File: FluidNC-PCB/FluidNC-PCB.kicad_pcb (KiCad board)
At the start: 2 copper layers, 133 x 92.5 mm, 51 parts, among them J1 Conn_01x04_Pin, J11 Molex_01x02_Socket, J12 Molex_01x02_Socket, J13 Molex_01x02_Socket, J14 Molex_01x02_Socket, J15 Molex_01x02_Socket, J16 Molex_01x02_Socket, J17 Molex_01x02_Socket, J18 Molex_01x02_Socket, J2 Conn_01x04_Pin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

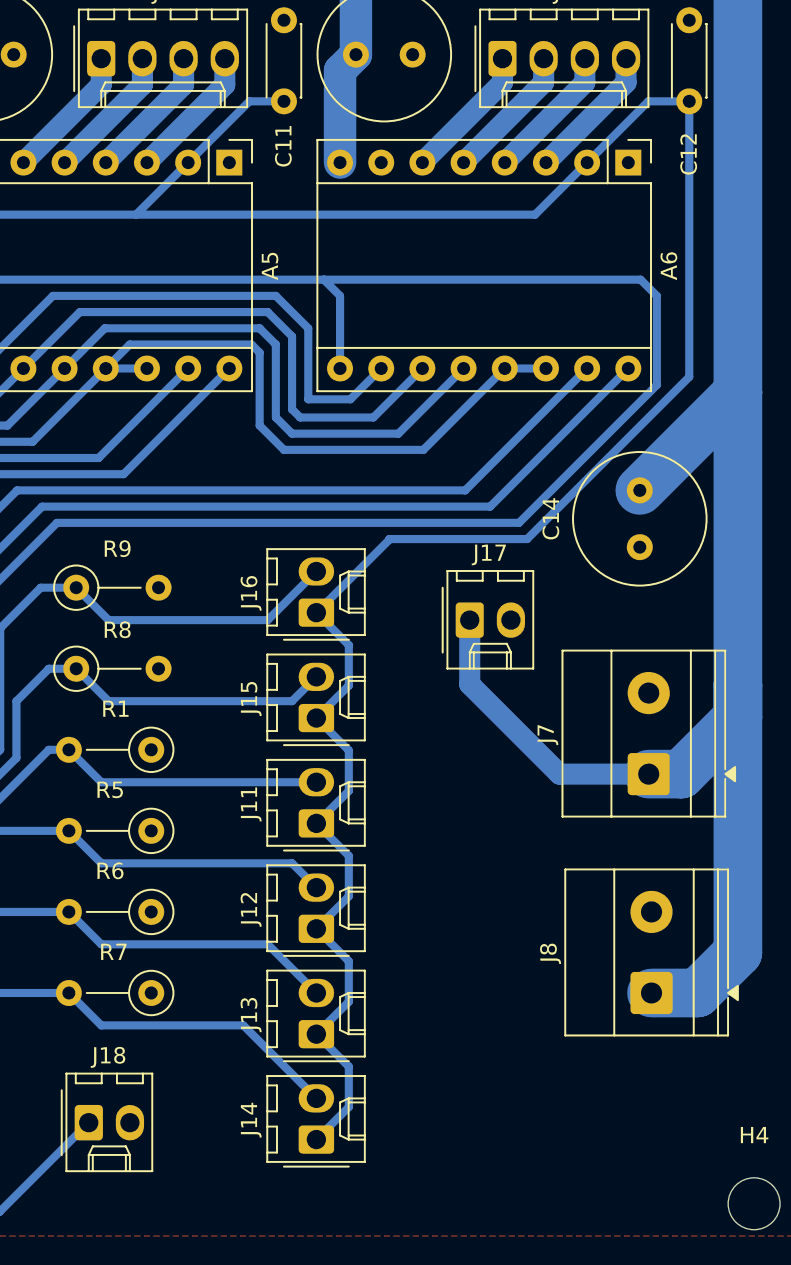
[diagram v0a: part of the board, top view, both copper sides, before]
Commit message: Small reroutes before github rename
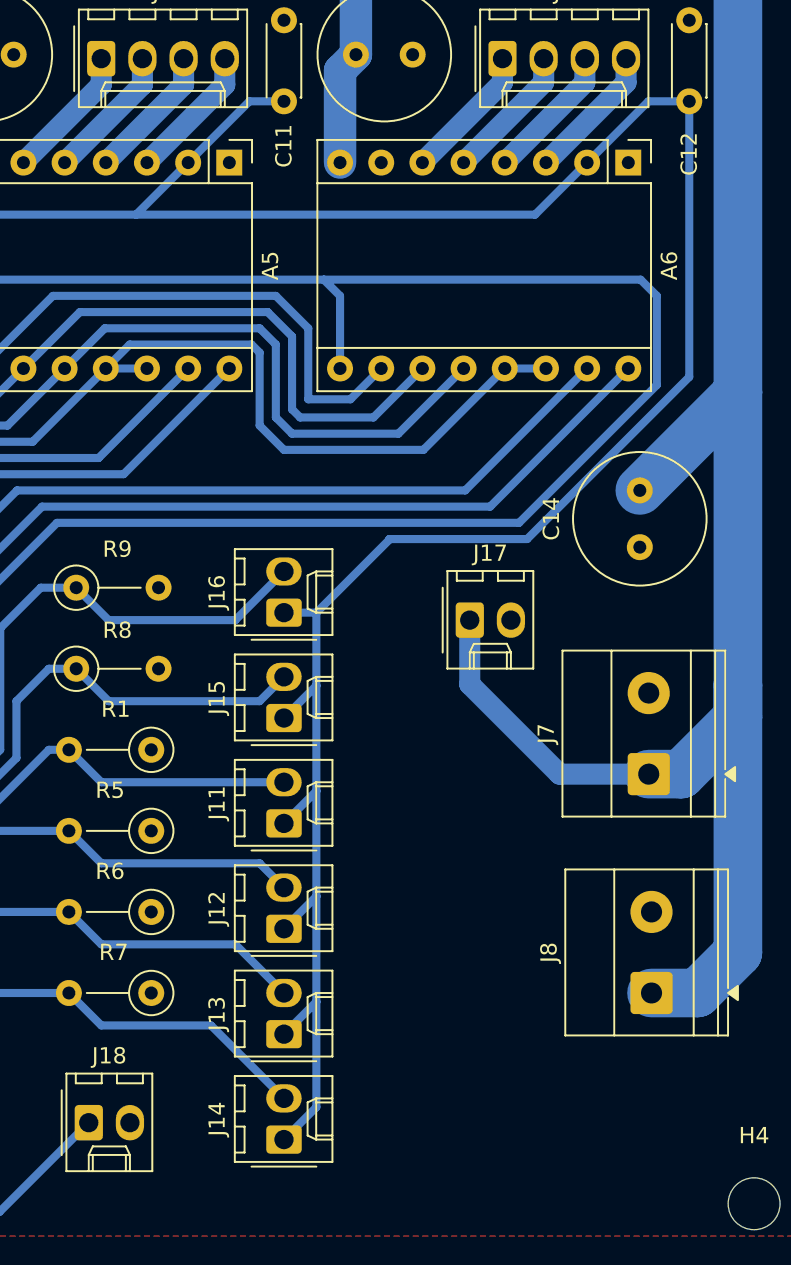
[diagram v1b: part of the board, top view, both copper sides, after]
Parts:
- moved J11 2.00 mm to (175.5, 118.0)
- moved J12 2.00 mm to (175.5, 124.5)
- moved J13 2.00 mm to (175.5, 131.0)
- moved J14 2.00 mm to (175.5, 137.5)
- moved J15 2.00 mm to (175.5, 111.5)
- moved J16 2.00 mm to (175.5, 105.0)
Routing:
- net +3.3V: track 594.9 -> 600.8 mm
- net Net-(J16-Pin_2): track 53.8 -> 51.8 mm
- net Net-(J15-Pin_2): track 50.5 -> 48.5 mm
- net Net-(J14-Pin_2): track 91.9 -> 89.9 mm
- net Net-(J13-Pin_2): track 96.8 -> 94.8 mm
- net Net-(J12-Pin_2): track 101.7 -> 99.7 mm
- net Net-(J11-Pin_2): track 104.6 -> 102.6 mm

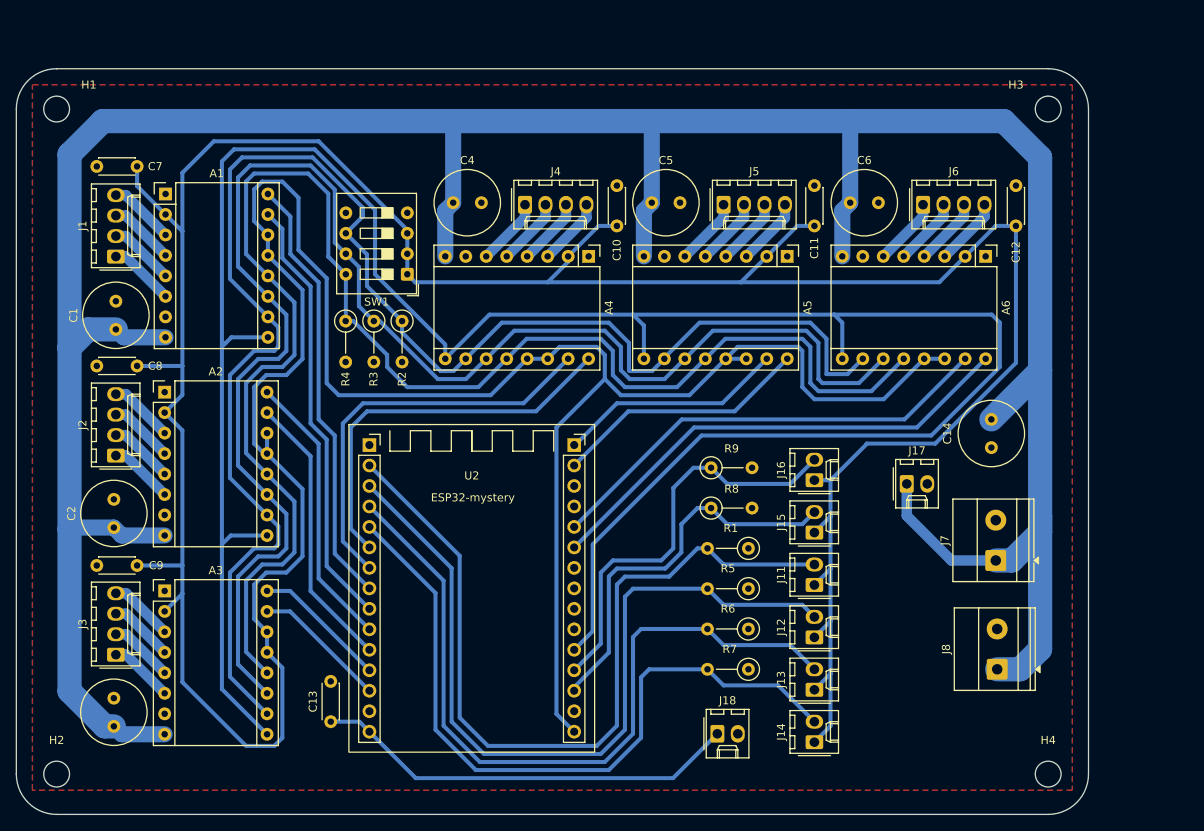
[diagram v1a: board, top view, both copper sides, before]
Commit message: Updated board with licensing and links to git repo
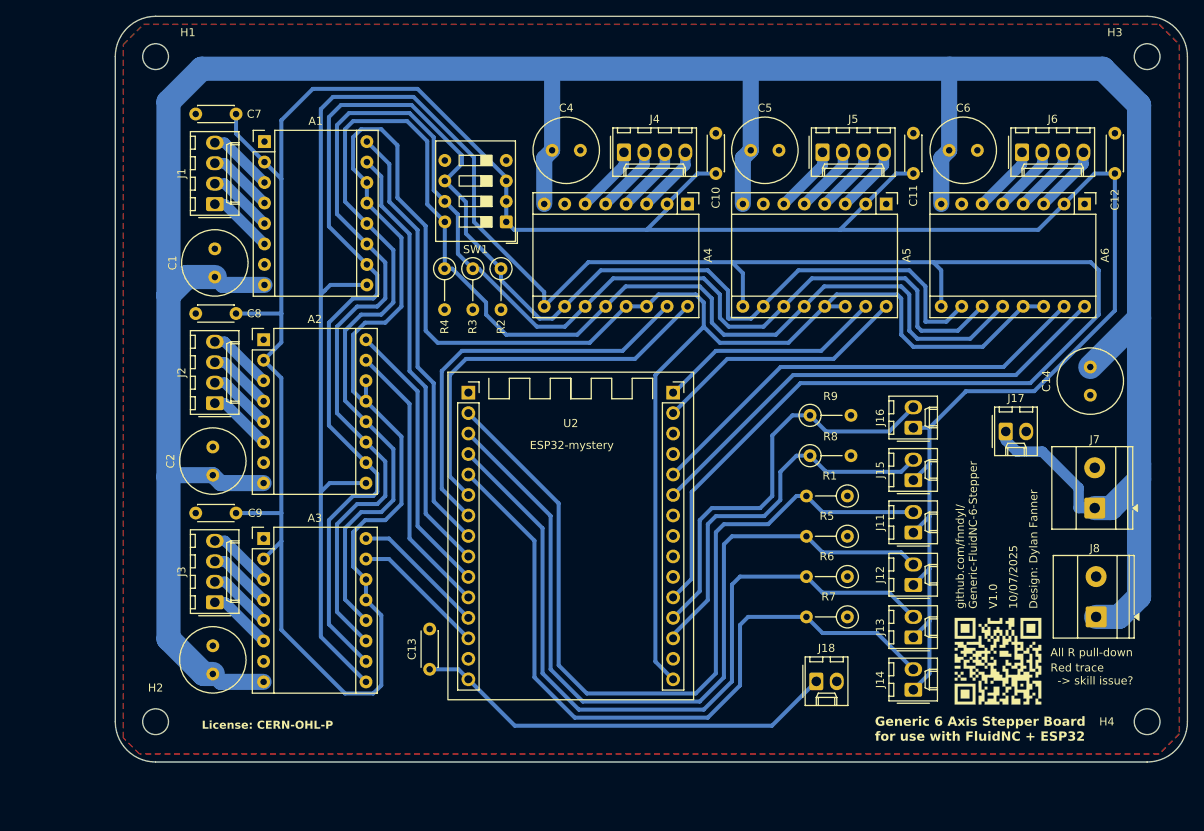
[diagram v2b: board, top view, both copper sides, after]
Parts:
- added G***: LOGO, plotter:qr_small, F.Cu at (198.3, 127.5)
- moved A5 13.9 mm to (184.4, 70.8)
- moved C1 13.9 mm to (101.1, 79.8)
- moved C10 13.9 mm to (163.3, 67.0)
- moved C11 13.9 mm to (187.8, 67.0)
- moved C12 13.9 mm to (212.8, 67.0)
- moved C13 13.9 mm to (127.8, 128.5)
- moved C14 13.9 mm to (209.7, 91.0)
- moved C2 13.9 mm to (100.9, 104.4)
- moved C3 13.9 mm to (100.9, 129.1)
- moved C4 13.9 mm to (143.0, 64.1)
- moved C6 13.9 mm to (192.2, 64.1)
- moved H1 13.9 mm to (93.8, 52.5)
- moved H2 13.9 mm to (93.8, 135.0)
- moved H3 13.9 mm to (216.8, 52.5)
- moved H4 13.9 mm to (216.8, 135.0)
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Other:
- board text added: "10/07/2025"
- board text added: "All R pull-down"
- board text added: "Design: Dylan Fanner"
- board text added: "Generic 6 Axis Stepper Board for use with FluidNC + ESP32"
- board text added: "License: CERN-OHL-P"
- board text added: "Red trace -> skill issue?"
- board text added: "V1.0"
- board text added: "github.com/fnndyl/ Generic-FluidNC-6-Stepper"
